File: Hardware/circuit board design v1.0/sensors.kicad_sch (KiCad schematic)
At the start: 1 part

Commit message: Changes on 14/02/2023
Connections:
- net GND: now reaches U?.1 (GND)
- net GND: now also U?.5 (SDO), U?.7 (GND)
- net +3.3V: now reaches U?.2 (CSB)
- net +3.3V: now also U?.6 (VDDIO)
- net SDA: now reaches U?.3 (SDI)
- net SCL: now reaches U?.4 (SCK)
- net +3.3VA: now reaches U?.8 (VDD)
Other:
- note added: "VDD is the analog voltage input and VDDIO is the digital"
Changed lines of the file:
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@@
 (kicad_sch (version 20211123) (generator eeschema)
   (paper "A4")
+  (junction (at 132.08 69.85) (diameter 0) (color 0 0 0 0)
+  )
+  (junction (at 132.08 105.41) (diameter 0) (color 0 0 0 0)
+  )
+  (wire (pts (xy 149.86 78.74) (xy 165.1 78.74))
+    (stroke (width 0) (type default) (color 0 0 0 0))
+  )
+  (wire (pts (xy 137.16 60.96) (xy 137.16 71.12))
+    (stroke (width 0) (type default) (color 0 0 0 0))
+  )
+  (wire (pts (xy 149.86 93.98) (xy 152.4 93.98))
+    (stroke (width 0) (type default) (color 0 0 0 0))
+  )
+  (wire (pts (xy 132.08 105.41) (xy 132.08 110.49))
+    (stroke (width 0) (type default) (color 0 0 0 0))
+  )
+  (wire (pts (xy 137.16 101.6) (xy 137.16 105.41))
+    (stroke (width 0) (type default) (color 0 0 0 0))
+  )
+  (wire (pts (xy 132.08 60.96) (xy 132.08 69.85))
+    (stroke (width 0) (type default) (color 0 0 0 0))
+  )
+  (wire (pts (xy 149.86 83.82) (xy 153.67 83.82))
+    (stroke (width 0) (type default) (color 0 0 0 0))
+  )
+  (wire (pts (xy 149.86 88.9) (xy 153.67 88.9))
+    (stroke (width 0) (type default) (color 0 0 0 0))
+  )
+  (wire (pts (xy 132.08 69.85) (xy 132.08 71.12))
+    (stroke (width 0) (type default) (color 0 0 0 0))
+  )
+  (wire (pts (xy 132.08 69.85) (xy 152.4 69.85))
+    (stroke (width 0) (type default) (color 0 0 0 0))
+  )
+  (wire (pts (xy 132.08 105.41) (xy 137.16 105.41))
+    (stroke (width 0) (type default) (color 0 0 0 0))
+  )
+  (wire (pts (xy 152.4 93.98) (xy 152.4 69.85))
+    (stroke (width 0) (type default) (color 0 0 0 0))
+  )
+  (wire (pts (xy 132.08 101.6) (xy 132.08 105.41))
+    (stroke (width 0) (type default) (color 0 0 0 0))
+  )
+  (text "VDD is the analog voltage input and VDDIO is the digital\n"
+    (at 144.78 67.31 0)
+    (effects (font (size 1.27 1.27)) (justify left bottom))
+  )
+  (hierarchical_label "SCL" (shape bidirectional) (at 153.67 83.82 0)
+    (effects (font (size 1.27 1.27)) (justify left))
+  )
+  (hierarchical_label "SDA" (shape bidirectional) (at 153.67 88.9 0)
+    (effects (font (size 1.27 1.27)) (justify left))
+  )
+  (symbol (lib_id "power:+3.3V") (at 132.08 60.96 0) (unit 1)
+    (in_bom yes) (on_board yes) (fields_autoplaced)
+    (property "Reference" "#PWR?" (id 0) (at 132.08 64.77 0)
+      (effects (font (size 1.27 1.27)) hide)
+    )
+    (property "Value" "+3.3V" (id 1) (at 132.08 55.88 0))
+    (property "Footprint" "" (id 2) (at 132.08 60.96 0)
+      (effects (font (size 1.27 1.27)) hide)
+    )
+    (property "Datasheet" "" (id 3) (at 132.08 60.96 0)
+      (effects (font (size 1.27 1.27)) hide)
+    )
+    (pin "1")
+  )
+  (symbol (lib_id "power:+3.3VA") (at 137.16 60.96 0) (unit 1)
+    (in_bom yes) (on_board yes)
+    (property "Reference" "#PWR?" (id 0) (at 137.16 64.77 0)
+      (effects (font (size 1.27 1.27)) hide)
+    )
+    (property "Value" "+3.3VA" (id 1) (at 137.16 55.88 0))
+    (property "Footprint" "" (id 2) (at 137.16 60.96 0)
+      (effects (font (size 1.27 1.27)) hide)
+    )
+    (property "Datasheet" "" (id 3) (at 137.16 60.96 0)
+      (effects (font (size 1.27 1.27)) hide)
+    )
+    (pin "1")
+  )
+  (symbol (lib_id "power:GND") (at 132.08 110.49 0) (unit 1)
+    (in_bom yes) (on_board yes) (fields_autoplaced)
+    (property "Reference" "#PWR?" (id 0) (at 132.08 116.84 0)
+      (effects (font (size 1.27 1.27)) hide)
+    )
+    (property "Value" "GND" (id 1) (at 132.08 115.57 0))
+    (property "Footprint" "" (id 2) (at 132.08 110.49 0)
+      (effects (font (size 1.27 1.27)) hide)
+    )
+    (property "Datasheet" "" (id 3) (at 132.08 110.49 0)
+      (effects (font (size 1.27 1.27)) hide)
+    )
+    (pin "1")
+  )
+  (symbol (lib_id "power:GND") (at 165.1 78.74 0) (unit 1)
+    (in_bom yes) (on_board yes) (fields_autoplaced)
+    (property "Reference" "#PWR?" (id 0) (at 165.1 85.09 0)
+      (effects (font (size 1.27 1.27)) hide)
+    )
+    (property "Value" "GND" (id 1) (at 165.1 83.82 0))
+    (property "Footprint" "" (id 2) (at 165.1 78.74 0)
+      (effects (font (size 1.27 1.27)) hide)
+    )
+    (property "Datasheet" "" (id 3) (at 165.1 78.74 0)
+      (effects (font (size 1.27 1.27)) hide)
+    )
+    (pin "1")
+  )
   (symbol (lib_id "Sensor:BME280") (at 134.62 86.36 0) (unit 1)
     (in_bom yes) (on_board yes) (fields_autoplaced)

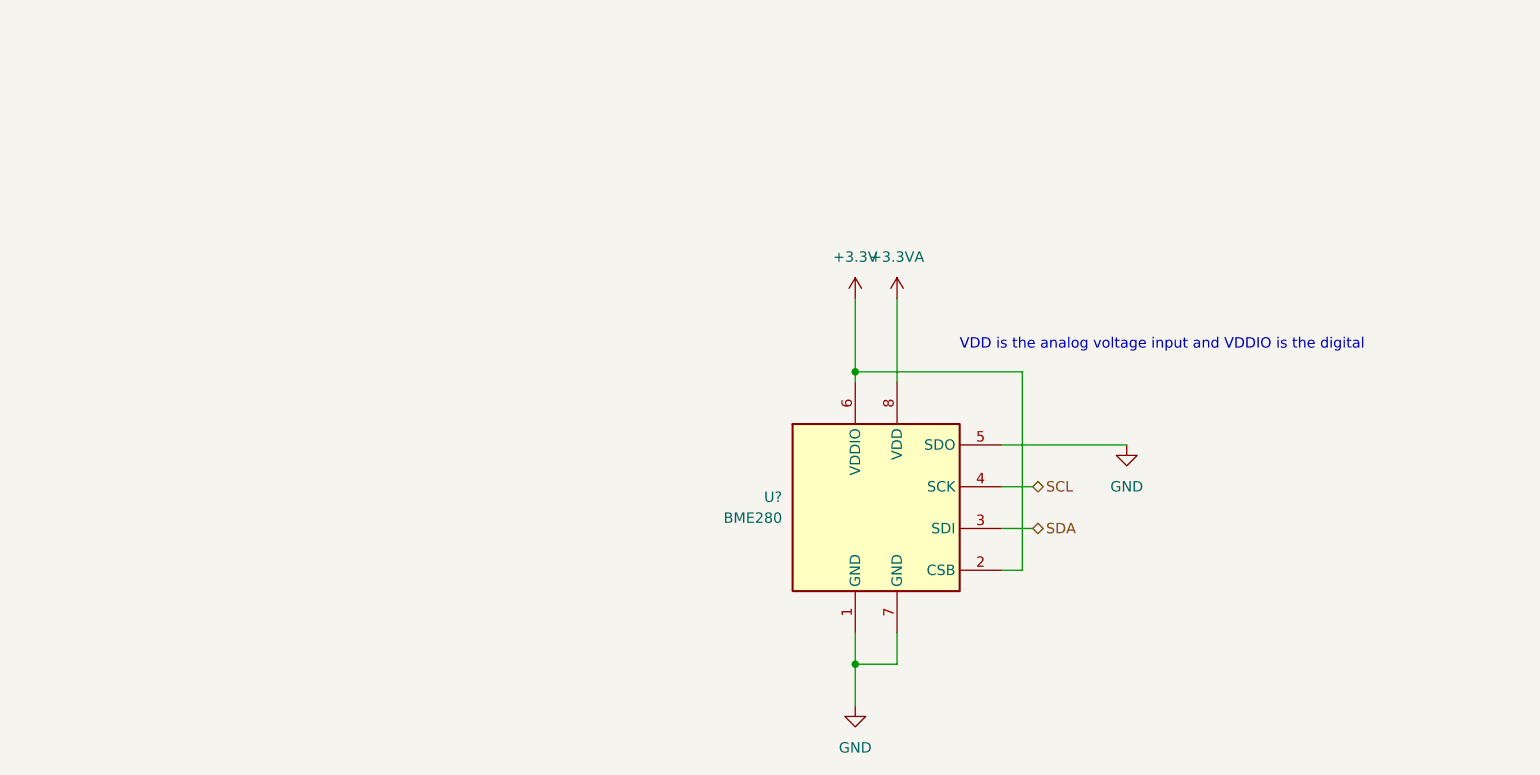
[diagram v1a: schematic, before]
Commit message: BMI088 schematic
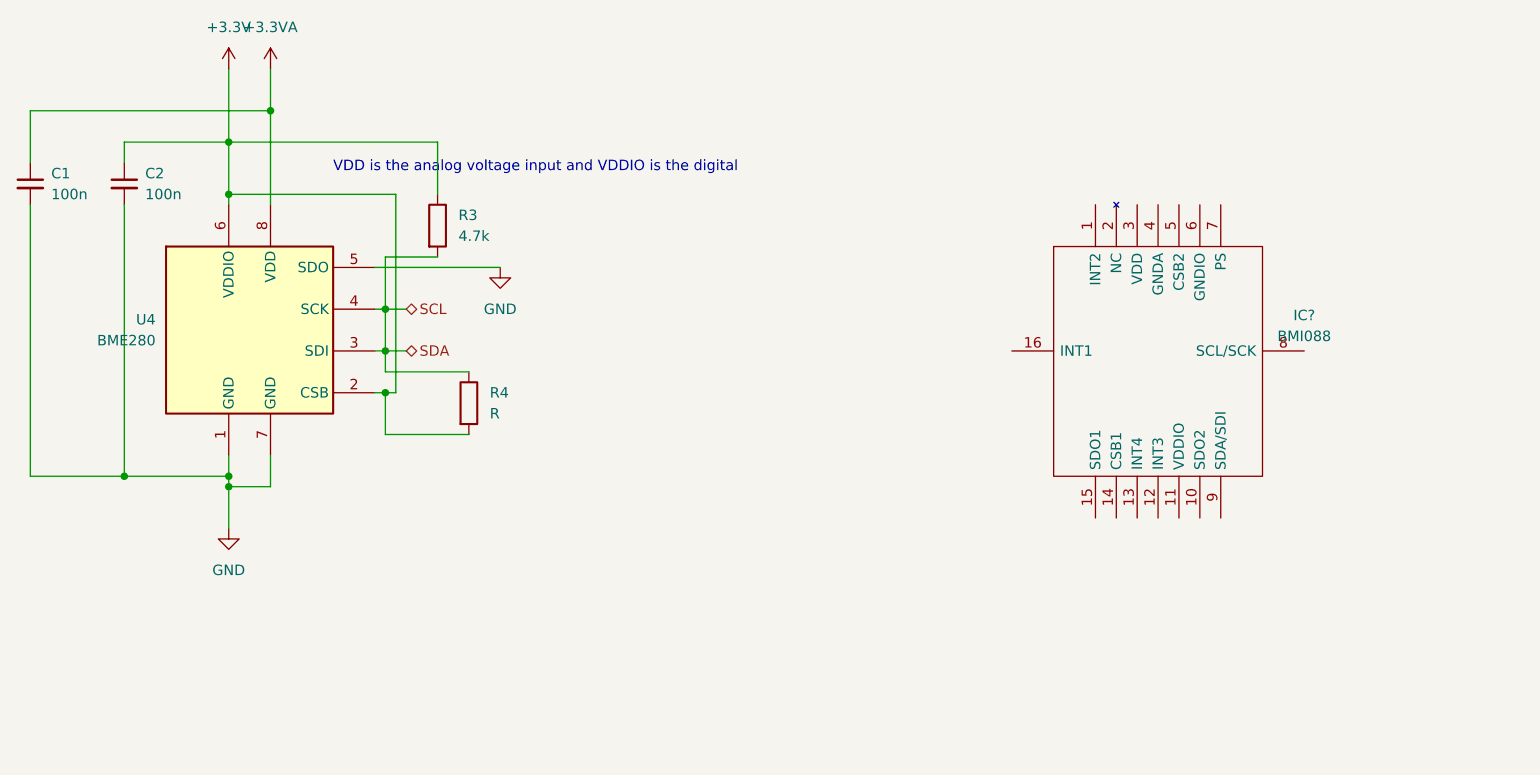
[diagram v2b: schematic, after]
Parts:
- added C1: 100n, symbol Device:C_Small
- added C2: 100n, Capacitor_SMD:C_0603_1608Metric_Pad1.08x0.95mm_HandSolder, symbol Device:C_Small
- added IC?: BMI088, Components:BMI088, symbol Components:BMI088
- added R3: 4.7k, symbol Device:R
- added R4: R, symbol Device:R
- gave numbers to parts that had none: 1
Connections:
- net SDA is gone; now on net SCL: U4.3 (SDI)
- net +3.3V: now also C2.1, R3.1, R4.2
- net +3.3VA: now also C1.1
- net GND: now also C1.2, C2.2
- net SCL: now also R3.2, R4.1
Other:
- moved on the sheet: U4

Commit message: Continued layout for PCB
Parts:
- added C? (x2): C_Small, Capacitor_SMD:C_0603_1608Metric, symbol Device:C_Small
- C1: footprint (none) -> Capacitor_SMD:C_0603_1608Metric
- C2: footprint Capacitor_SMD:C_0603_1608Metric_Pad1.08x0.95mm_HandSolder -> Capacitor_SMD:C_0603_1608Metric
- R3: footprint (none) -> Resistor_SMD:R_0603_1608Metric
- R4: value R -> 4.7k; footprint (none) -> Resistor_SMD:R_0603_1608Metric
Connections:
- net +3.3V: now also IC?.11 (VDDIO), IC?.7 (PS), C?.2
- net +3.3VA: now also IC?.3 (VDD), C?.1
- net GND: now also IC?.10 (SDO2), IC?.15 (SDO1), IC?.4 (GNDA), IC?.6 (GNDIO), C?.1, C?.2
- net SCL: now also IC?.8 (SCL/SCK), IC?.9 (SDA/SDI)
- no-connect marks 0 -> 6
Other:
- note added: "Accelerometer: SDO1 pin pulled to ground: 0x18 Gyroscope: SDO2 pin pulled to ground: 0x68"
- note added: "Pin 7 (PS) has to be high to select I2C for Gyro. By default the accelerometer uses I2C uncless there is a rising edge on Pin 14 (CSB1)"
- moved on the sheet: C1, C2, R4

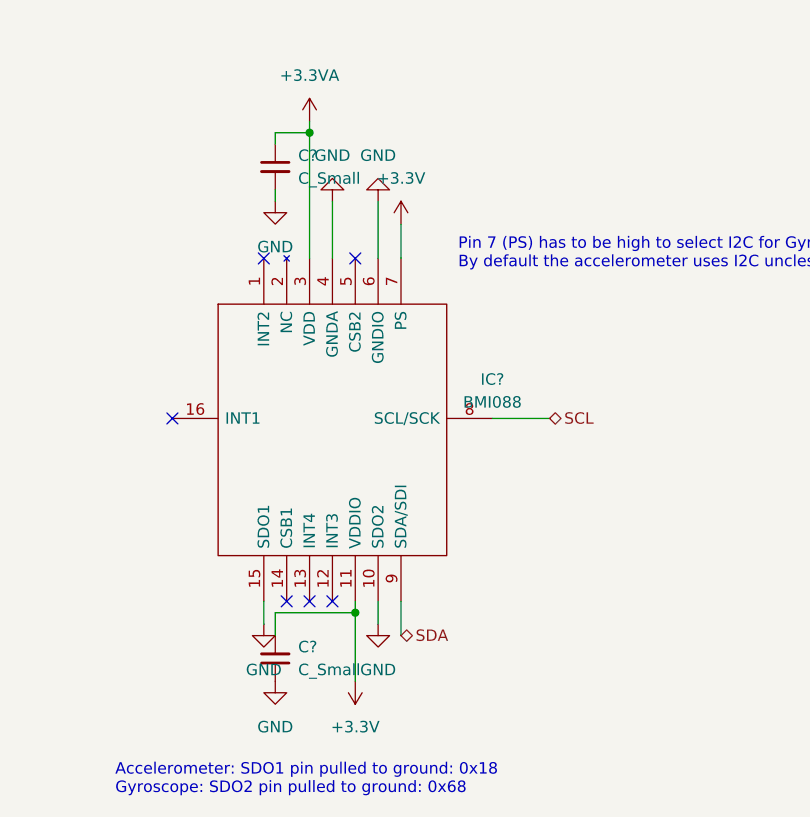
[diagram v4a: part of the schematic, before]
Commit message: Created stm32mx project and started on layout
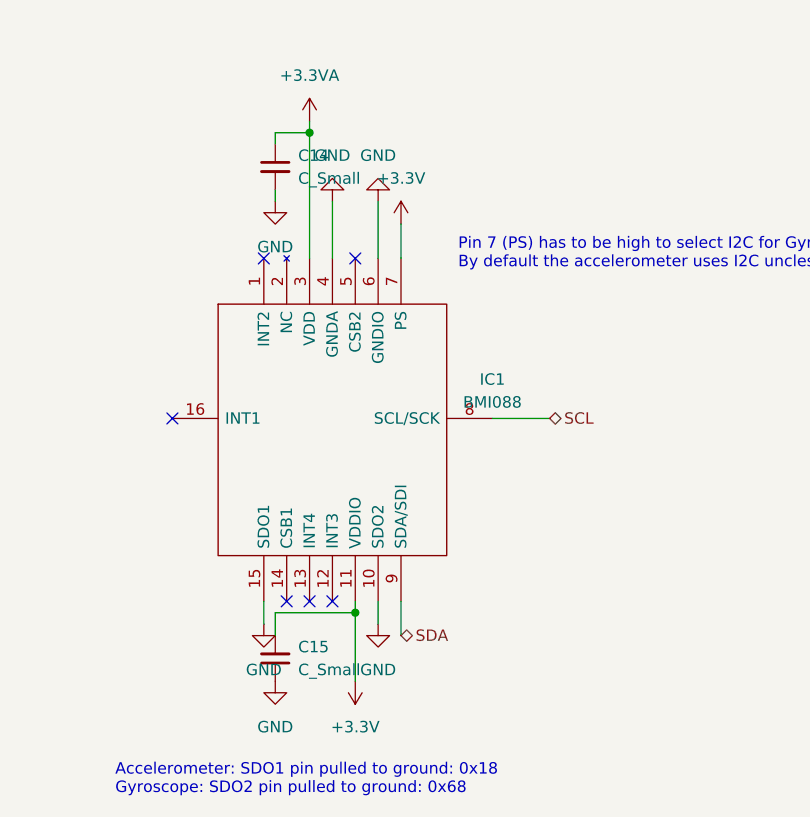
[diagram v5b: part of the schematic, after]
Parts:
- gave numbers to parts that had none: 3
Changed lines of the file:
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@@
   (symbol (lib_id "power:+3.3VA") (at 166.37 34.29 0) (unit 1)
     (in_bom yes) (on_board yes) (fields_autoplaced)
-    (property "Reference" "#PWR?" (id 0) (at 166.37 38.1 0)
+    (property "Reference" "#PWR0143" (id 0) (at 166.37 38.1 0)
       (effects (font (size 1.27 1.27)) hide)
     )
@@
   (symbol (lib_id "power:+3.3V") (at 171.45 96.52 180) (unit 1)
     (in_bom yes) (on_board yes) (fields_autoplaced)
-    (property "Reference" "#PWR?" (id 0) (at 171.45 92.71 0)
+    (property "Reference" "#PWR0137" (id 0) (at 171.45 92.71 0)
       (effects (font (size 1.27 1.27)) hide)
     )
@@
   (symbol (lib_id "power:GND") (at 162.56 43.18 0) (unit 1)
     (in_bom yes) (on_board yes) (fields_autoplaced)
-    (property "Reference" "#PWR?" (id 0) (at 162.56 49.53 0)
+    (property "Reference" "#PWR0139" (id 0) (at 162.56 49.53 0)
       (effects (font (size 1.27 1.27)) hide)
     )
@@
   (symbol (lib_id "power:GND") (at 168.91 43.18 180) (unit 1)
     (in_bom yes) (on_board yes) (fields_autoplaced)
-    (property "Reference" "#PWR?" (id 0) (at 168.91 36.83 0)
+    (property "Reference" "#PWR0140" (id 0) (at 168.91 36.83 0)
       (effects (font (size 1.27 1.27)) hide)
     )
@@
   (symbol (lib_id "Components:BMI088") (at 151.13 67.31 0) (unit 1)
     (in_bom yes) (on_board yes) (fields_autoplaced)
-    (property "Reference" "IC?" (id 0) (at 186.69 62.9793 0))
+    (property "Reference" "IC1" (id 0) (at 186.69 62.9793 0))
     (property "Value" "BMI088" (id 1) (at 186.69 65.5193 0))
     (property "Footprint" "Components:BMI088" (id 2) (at 182.88 54.61 0)
@@
   (symbol (lib_id "power:GND") (at 173.99 90.17 0) (unit 1)
     (in_bom yes) (on_board yes) (fields_autoplaced)
-    (property "Reference" "#PWR?" (id 0) (at 173.99 96.52 0)
+    (property "Reference" "#PWR0138" (id 0) (at 173.99 96.52 0)
       (effects (font (size 1.27 1.27)) hide)
     )
@@
   (symbol (lib_id "power:GND") (at 173.99 43.18 180) (unit 1)
     (in_bom yes) (on_board yes) (fields_autoplaced)
-    (property "Reference" "#PWR?" (id 0) (at 173.99 36.83 0)
+    (property "Reference" "#PWR0141" (id 0) (at 173.99 36.83 0)
       (effects (font (size 1.27 1.27)) hide)
     )
@@
   (symbol (lib_id "power:GND") (at 69.85 39.37 0) (unit 1)
     (in_bom yes) (on_board yes) (fields_autoplaced)
-    (property "Reference" "#PWR?" (id 0) (at 69.85 45.72 0)
+    (property "Reference" "#PWR0144" (id 0) (at 69.85 45.72 0)
       (effects (font (size 1.27 1.27)) hide)
     )
@@
   (symbol (lib_id "Device:C_Small") (at 162.56 39.37 0) (unit 1)
     (in_bom yes) (on_board yes) (fields_autoplaced)
-    (property "Reference" "C?" (id 0) (at 165.1 38.1062 0)
+    (property "Reference" "C14" (id 0) (at 165.1 38.1062 0)
       (effects (font (size 1.27 1.27)) (justify left))
     )
@@
   (symbol (lib_id "power:GND") (at 162.56 96.52 0) (unit 1)
     (in_bom yes) (on_board yes) (fields_autoplaced)
-    (property "Reference" "#PWR?" (id 0) (at 162.56 102.87 0)
+    (property "Reference" "#PWR0136" (id 0) (at 162.56 102.87 0)
       (effects (font (size 1.27 1.27)) hide)
     )
@@
   (symbol (lib_id "power:+3.3V") (at 176.53 45.72 0) (unit 1)
     (in_bom yes) (on_board yes) (fields_autoplaced)
-    (property "Reference" "#PWR?" (id 0) (at 176.53 49.53 0)
+    (property "Reference" "#PWR0142" (id 0) (at 176.53 49.53 0)
       (effects (font (size 1.27 1.27)) hide)
     )
@@
   (symbol (lib_id "power:GND") (at 48.26 39.37 0) (unit 1)
     (in_bom yes) (on_board yes) (fields_autoplaced)
-    (property "Reference" "#PWR?" (id 0) (at 48.26 45.72 0)
+    (property "Reference" "#PWR0145" (id 0) (at 48.26 45.72 0)
       (effects (font (size 1.27 1.27)) hide)
     )
@@
   (symbol (lib_id "power:GND") (at 161.29 90.17 0) (unit 1)
     (in_bom yes) (on_board yes) (fields_autoplaced)
-    (property "Reference" "#PWR?" (id 0) (at 161.29 96.52 0)
+    (property "Reference" "#PWR0135" (id 0) (at 161.29 96.52 0)
       (effects (font (size 1.27 1.27)) hide)
     )
@@
   (symbol (lib_id "Device:C_Small") (at 162.56 93.98 180) (unit 1)
     (in_bom yes) (on_board yes) (fields_autoplaced)
-    (property "Reference" "C?" (id 0) (at 165.1 92.7035 0)
+    (property "Reference" "C15" (id 0) (at 165.1 92.7035 0)
       (effects (font (size 1.27 1.27)) (justify right))
     )
